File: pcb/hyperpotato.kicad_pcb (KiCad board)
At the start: 2 copper layers, 117 x 88.3 mm, 46 parts, among them J1 Conn_01x02_Socket, J2 Conn_01x03_Pin, Q1 AO3401A, SW1 SW_Push_45deg, SW10 SW_Push_45deg, SW11 SW_Push_45deg, SW12 SW_Push_45deg, SW13 SW_Push_45deg, SW14 SW_SPDT, SW15 SW_Push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

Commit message: Route haptic driver
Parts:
- U1: footprint ssbb_parts:Xiao_nRF52840_AC_Reflow_reversible -> hyperpotato:Xiao_nRF52840_AC_Reflow_reversible
- moved U4 61.0 mm to (140.2, 87.3), turned to 180 degrees
- moved U1 16.7 mm to (145.1, 61.4), turned to 0 degrees
- moved SW14 16.5 mm to (165.5, 54.3), turned to 180 degrees
- moved SW1 15.5 mm to (165.5, 67.0), turned to 0 degrees
- moved SW2 15.3 mm to (187.2, 61.0), turned to -5 degrees
- moved SW15 15.3 mm to (205.6, 56.8), turned to 175 degrees
- moved U5 15.2 mm to (145.1, 79.4), turned to -90 degrees
- moved D14 15.1 mm to (220.3, 57.2), turned to -140 degrees
- moved R6 14.8 mm to (216.0, 60.7), turned to -50 degrees
- moved D15 14.7 mm to (223.8, 61.4), turned to -140 degrees
- moved R7 14.4 mm to (219.6, 65.0), turned to -50 degrees
- moved D16 14.3 mm to (227.4, 65.7), turned to -140 degrees
- moved SW3 14.3 mm to (204.5, 69.4), turned to 175 degrees
- moved SW6 14.2 mm to (165.5, 84.0), turned to 0 degrees
- moved R8 14.0 mm to (223.1, 69.3), turned to -50 degrees
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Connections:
- U5 pad 1: COL0 -> COL3
- U5 pad 15: LED1 -> COL0
- U5 pad 3: COL3 -> LED3
- U5 pad 4: COL2 -> LED2
- U5 pad 5: COL1 -> LED1
- U5 pad 6: LED2 -> COL2
- U5 pad 7: LED3 -> COL1
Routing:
- net +3.3V: track 11.1 -> 98.7 mm, vias 0 -> 8
- net ROW0: track 111.7 -> 164.3 mm, vias 5 -> 7
- net ROW2: track 112.8 -> 163.7 mm, vias 5 -> 7
- net ROW1: track 117.7 -> 168.2 mm, vias 7 -> 9
- net IO_CS: track 0.00 -> 43.0 mm, vias 0 -> 2
- net LED1: track 47.1 -> 90.0 mm, vias 1 -> 2
- net LED2: track 51.2 -> 91.8 mm, vias 1 -> 2
- net SCK: track 0.00 -> 40.6 mm, vias 0 -> 2
- net LED3: track 55.6 -> 96.1 mm, vias 1 -> 2
- net MOSI: track 0.00 -> 39.6 mm, vias 0 -> 2
- net COL0: track 2.27 -> 39.7 mm, vias 0 -> 1
- net TP_DATA: track 0.00 -> 37.0 mm, vias 0 -> 2
- net RESET: track 43.2 -> 79.0 mm, vias 1 -> 3
- net TP_CLK: track 0.00 -> 32.7 mm, vias 0 -> 2
- net TP_RST: track 0.00 -> 28.6 mm, vias 0 -> 2
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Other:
- board size 117 x 88.3 mm -> 115 x 90.8 mm

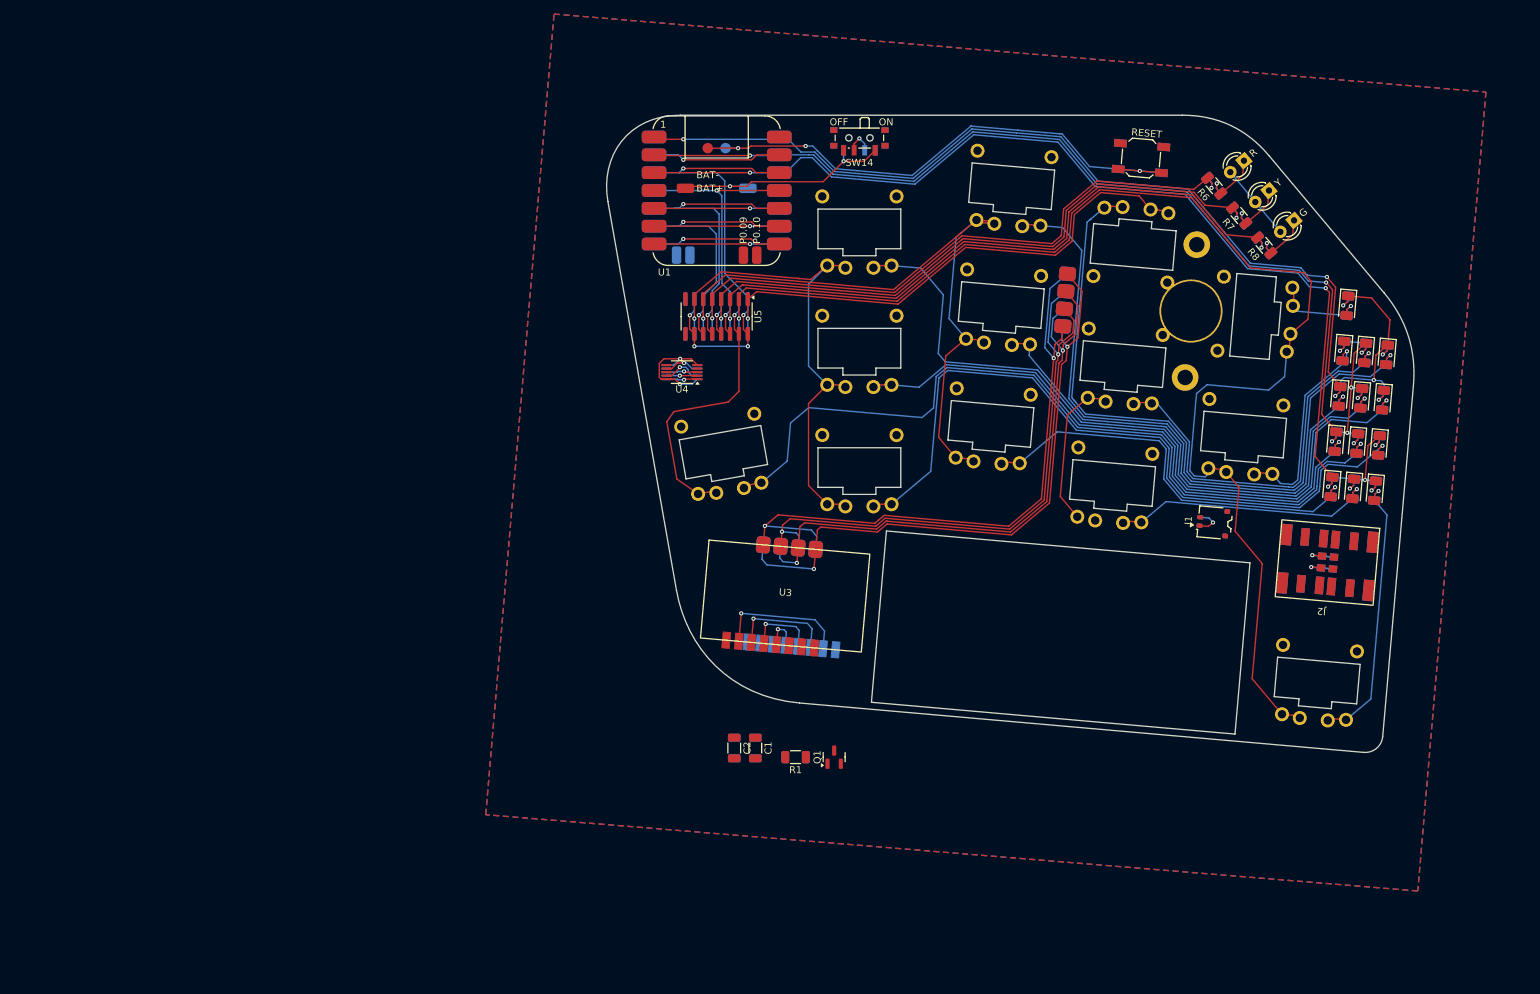
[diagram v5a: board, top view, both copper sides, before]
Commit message: Almost routed, changing 595 package
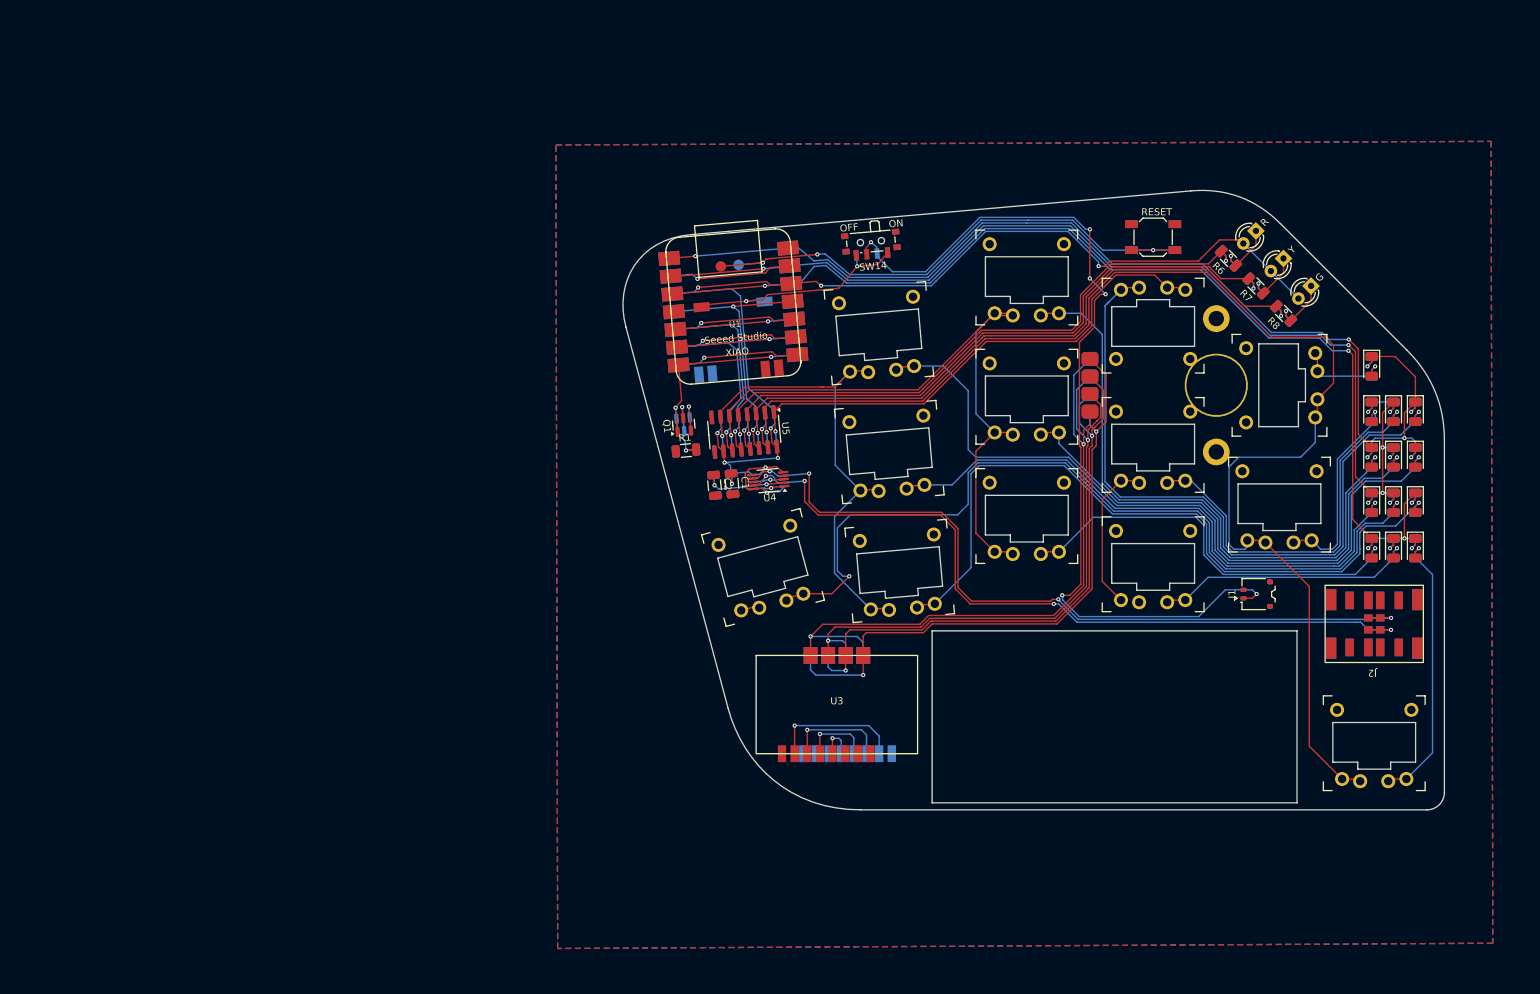
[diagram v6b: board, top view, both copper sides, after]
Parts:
- Q1: footprint Package_TO_SOT_SMD:SOT-23 -> hyperpotato:SOT-23_reversible
- SW1, SW10, SW11, SW12, SW13, SW2, SW3, SW4, SW5, SW6, SW7, SW8, SW9: footprint ssbb_parts:SW_Choc_Mini_reversible_1u -> hyperpotato:SW_Choc_Mini_reversible_1u
- U1: footprint hyperpotato:Xiao_nRF52840_AC_Reflow_reversible -> hyperpotato:XIAO-nRF52840-Sense-14P-2.54-21X17.8MM_1
- moved Q1 52.0 mm to (140.4, 94.8), turned to 95 degrees
- moved R1 46.4 mm to (140.8, 98.5), turned to 5 degrees
- moved C2 37.9 mm to (144.8, 103.4), turned to -85 degrees
- moved C1 37.6 mm to (147.3, 103.2), turned to -85 degrees
- moved U4 19.8 mm to (152.5, 102.8), turned to -175 degrees
- moved SW5 17.2 mm to (151.7, 115.1), turned to 15 degrees
- moved U3 17.1 mm to (162.3, 134.7), turned to 0 degrees
- moved U5 16.9 mm to (149.1, 95.8), turned to -85 degrees
- moved U1 16.7 mm to (147.5, 78.0), turned to 5 degrees
- moved SW10 15.7 mm to (171.2, 115.6), turned to 5 degrees
- moved SW6 15.3 mm to (169.7, 98.7), turned to 5 degrees
- moved SW1 15.0 mm to (168.2, 81.8), turned to 5 degrees
- moved SW14 14.9 mm to (167.1, 69.1), turned to -175 degrees
- moved SW11 14.0 mm to (189.3, 107.8), turned to 0 degrees
- moved SW7 13.4 mm to (189.3, 90.8), turned to 0 degrees
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- renumbered C2 to C1, C1 to C2
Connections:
- C1 pad 1: Net-(U4-REG) -> +3.3V
- C2 pad 1: +3.3V -> Net-(U4-REG)
- U3 pad 5: +3.3V -> +3.3V_OPTIONAL
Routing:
- net VBAT: track 8.23 -> 129.2 mm, vias 2 -> 6
- net Net-(J2-Pin_2): track 11.3 -> 111.1 mm, vias 2 -> 4
- net Net-(J2-Pin_1): track 12.0 -> 111.1 mm, vias 2 -> 4
- net +3.3V: track 98.7 -> 177.2 mm, vias 8 -> 11
- net COL0: track 39.7 -> 7.75 mm
- net POWER_CUTOFF: track 17.8 -> 37.2 mm, vias 1 -> 3
- net +3.3V_OPTIONAL: track 0.00 -> 10.5 mm, vias 0 -> 2
- net Net-(U4-REG): track 4.48 -> 13.3 mm, vias 1 -> 2
- net Net-(D5-A): track 117.0 -> 120.7 mm, vias 1 -> 2
- net ROW0: track 164.3 -> 162.3 mm
- net RESET: track 79.0 -> 80.7 mm
- net COL4: track 188.0 -> 186.4 mm
- net LED1: track 90.0 -> 88.7 mm
- net +BATT: track 33.5 -> 32.3 mm
- net LED3: track 96.1 -> 95.1 mm
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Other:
- board size 115 x 90.8 mm -> 117 x 88.3 mm

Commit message: Good progress on routing
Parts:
- U5: footprint ssbb_parts_reversible:SOIC-16_3.9x9.9mm_P1.27mm_reversible -> ssbb_parts_reversible:TSSOP-16_4.4x5mm_P0.65mm_reversible
- moved R1 13.5 mm to (151.7, 106.3), turned to 0 degrees
- moved Q1 13.5 mm to (151.7, 102.1), turned to 90 degrees
- moved U5 9.86 mm to (158.2, 99.5), turned to -90 degrees
- moved U4 6.71 mm to (148.5, 97.4), turned to 0 degrees
- moved C1 3.81 mm to (148.4, 102.1), turned to -90 degrees
- moved D2 3.51 mm to (241.4, 101.3)
- moved J1 3.51 mm to (225.0, 120.8)
- moved SW8 3.51 mm to (210.3, 99.6)
- moved D13 3.51 mm to (247.6, 114.3)
- moved SW14 3.51 mm to (170.1, 71.0)
- moved SW5 3.51 mm to (154.7, 117.0)
- moved R8 3.51 mm to (228.8, 80.9)
- moved SW6 3.51 mm to (172.7, 100.6)
- moved SW15 3.51 mm to (210.3, 70.0)
- moved D15 3.51 mm to (228.8, 73.0)
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- renumbered C2 to C1, C1 to C2
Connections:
- C1 pad 1: Net-(U4-REG) -> +3.3V
- C2 pad 1: +3.3V -> Net-(U4-REG)
- U1 pad 11: MOSI -> SCK
- U1 pad 13: SCK -> MOSI
- U1 pad 14: TP_RST -> POWER_CUTOFF
- U1 pad 7: POWER_CUTOFF -> TP_RST
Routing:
- net TP_DATA: track 37.0 -> 100.9 mm
- net TP_CLK: track 32.7 -> 93.0 mm
- net TP_RST: track 28.6 -> 87.3 mm
- net +3.3V_OPTIONAL: track 10.5 -> 61.5 mm
- net +3.3V: track 177.2 -> 198.6 mm, vias 11 -> 12
- net COL1: track 72.8 -> 90.3 mm
- net MOSI: track 39.6 -> 55.1 mm, vias 2 -> 3
- net Net-(J2-Pin_1): track 111.1 -> 126.3 mm
- net SCK: track 40.1 -> 55.2 mm, vias 2 -> 3
- net Net-(J2-Pin_2): track 111.1 -> 124.6 mm
- net COL2: track 96.1 -> 108.9 mm
- net LED1: track 88.7 -> 101.4 mm
- net IO_CS: track 43.0 -> 55.4 mm, vias 2 -> 3
- net SDA: track 4.48 -> 16.3 mm, vias 1 -> 2
- net LED2: track 91.1 -> 101.1 mm
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
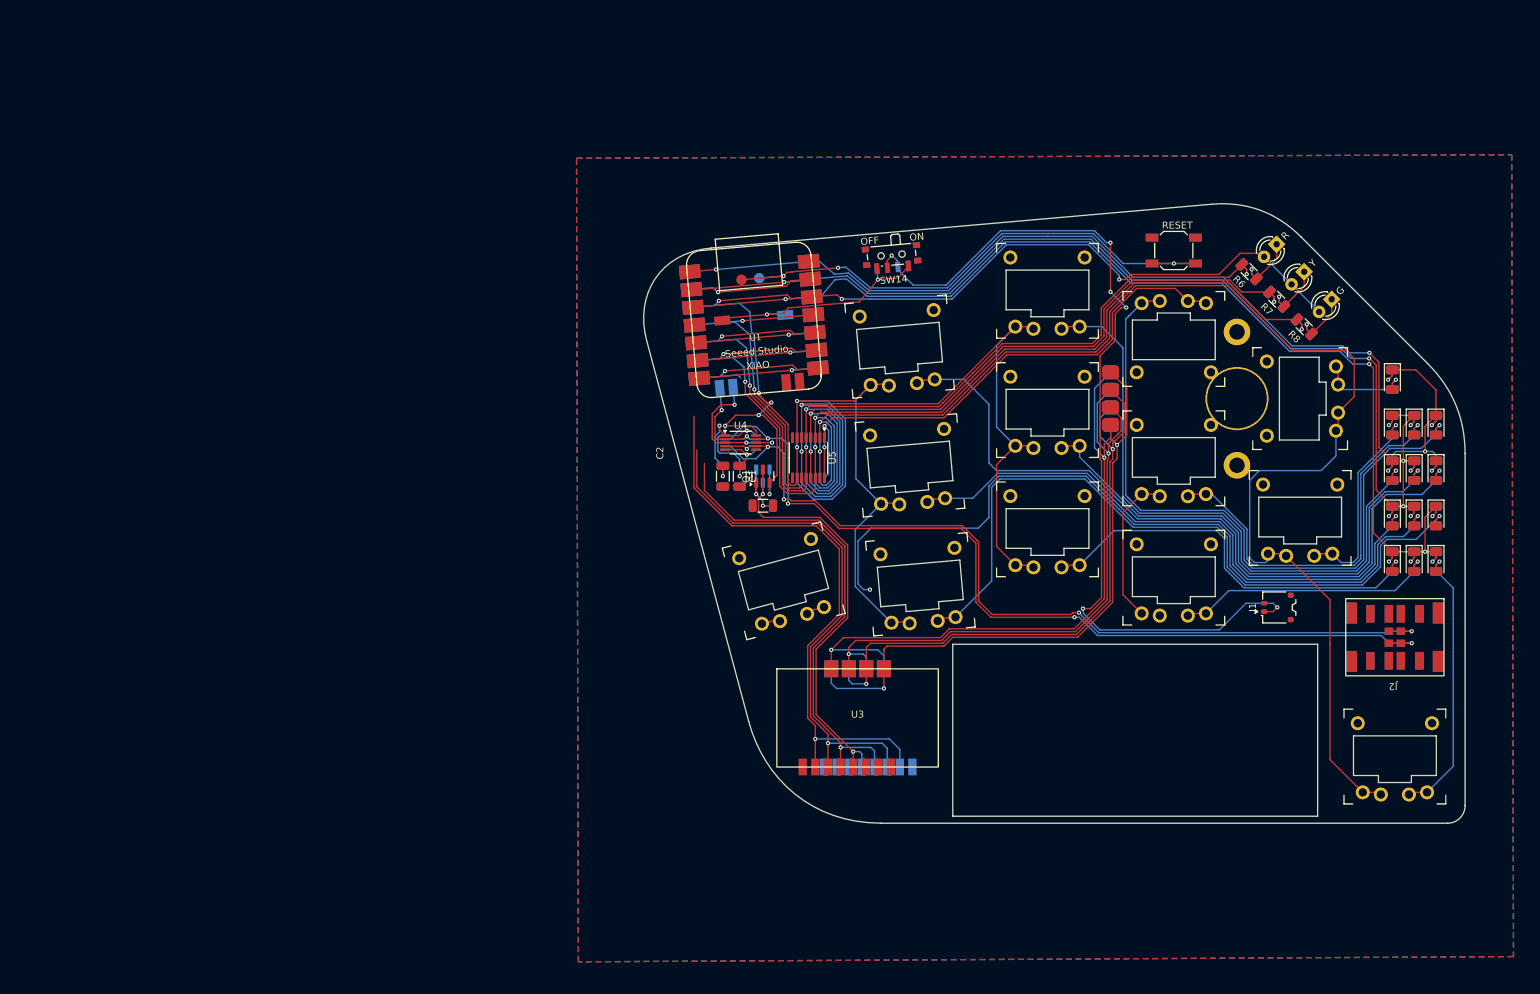
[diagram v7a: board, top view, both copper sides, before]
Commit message: Use in-house footprints,
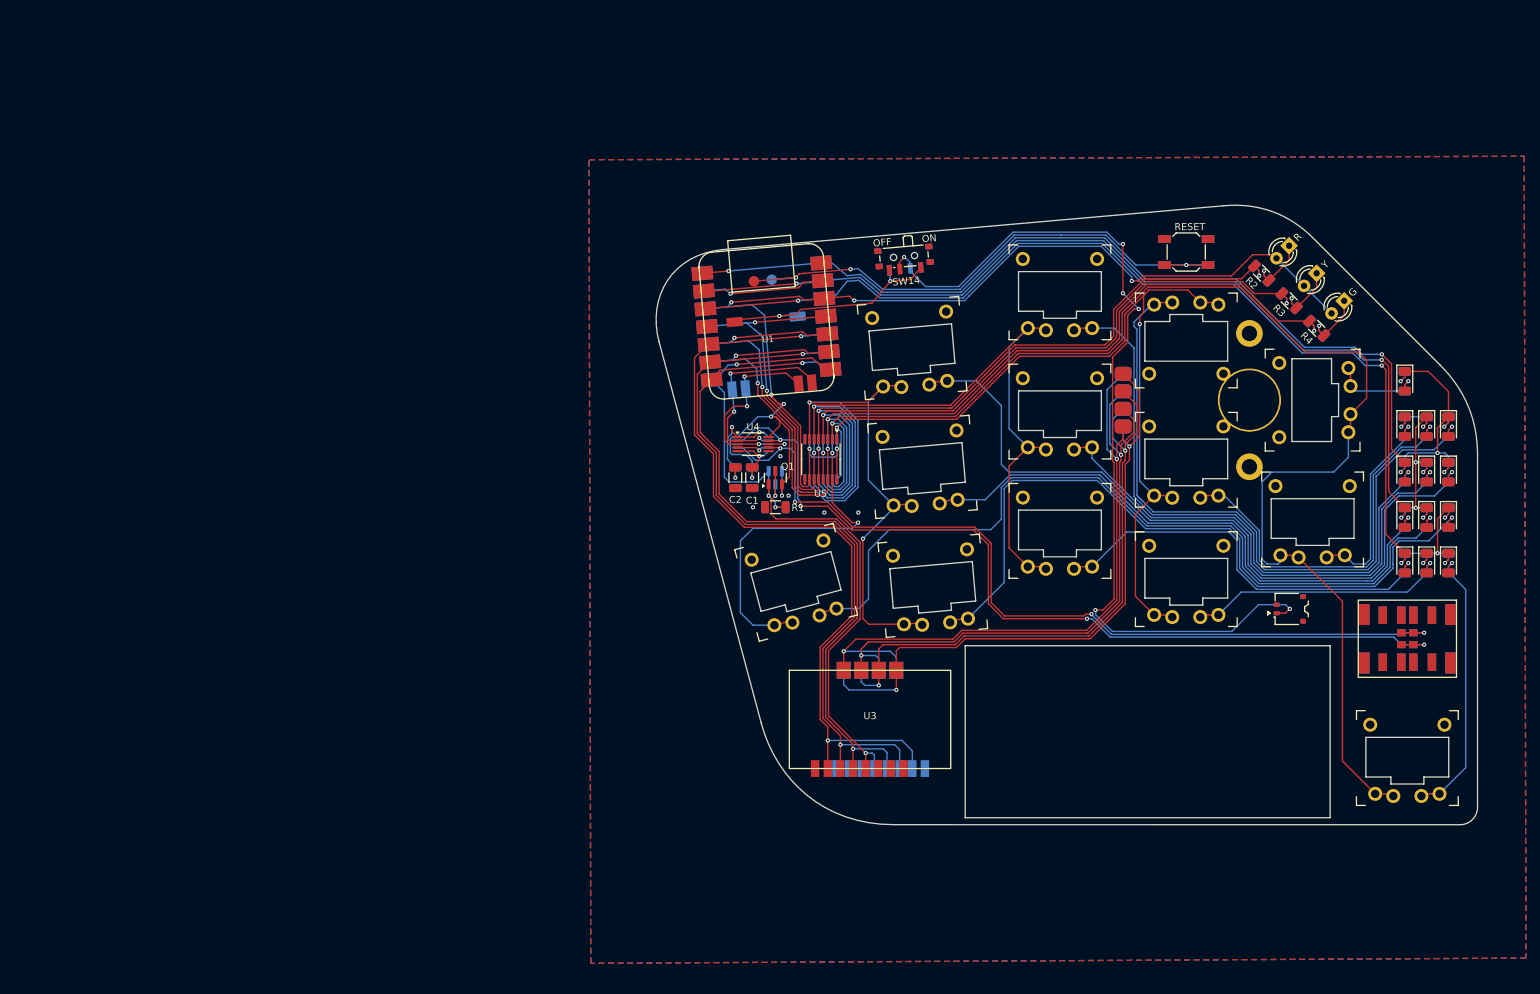
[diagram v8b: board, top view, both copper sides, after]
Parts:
- D9: moved to F.Cu
- H1: value MountingHole -> T460S
- U1: footprint hyperpotato:XIAO-nRF52840-Sense-14P-2.54-21X17.8MM_1 -> hyperpotato:XIAO-nRF52840-Sense-14P-2.54-21X17.8MM_reversible
- moved D2 1.79 mm to (243.2, 101.6)
- moved SW15 1.79 mm to (212.0, 70.2)
- moved D4 1.79 mm to (243.2, 88.6)
- moved R2 1.79 mm to (222.8, 73.2)
- moved SW5 1.79 mm to (156.5, 117.3)
- moved R1 1.79 mm to (153.5, 106.6)
- moved J1 1.79 mm to (226.8, 121.1)
- moved SW2 1.79 mm to (194.0, 75.9)
- moved Q1 1.79 mm to (153.5, 102.4)
- moved U1 1.79 mm to (152.2, 80.1)
- moved SW10 1.79 mm to (175.9, 117.8)
- moved SW1 1.79 mm to (173.0, 83.9)
- moved D11 1.79 mm to (243.2, 114.5)
- moved D16 1.79 mm to (234.5, 77.1)
- moved D8 1.79 mm to (246.3, 95.1)
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- renumbered R6 to R2, R7 to R3, R8 to R4
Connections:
- U1 pad 17: SCL -> SDA
- U1 pad 18: SDA -> SCL
- U1 pad 5: TP_CLK -> TP_DATA
- U1 pad 6: TP_DATA -> TP_CLK
- U3 pad 10: TP_S2 -> TP_GND
- U3 pad 11: TP_S3 -> TP_Y
- U3 pad 12: TP_S4 -> TP_X
- U3 pad 9: TP_S1 -> TP_VCC
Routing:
- net COL0: track 7.99 -> 49.8 mm, vias 1 -> 2
- net COL3: track 96.1 -> 128.2 mm, vias 1 -> 2
- net POWER_CUTOFF: track 31.6 -> 49.2 mm
- net SCL: track 13.7 -> 28.2 mm, vias 2 -> 3
- net TP_CLK: track 93.0 -> 107.5 mm
- net TP_RST: track 87.3 -> 101.0 mm
- net TP_DATA: track 100.9 -> 113.2 mm
- net SDA: track 16.3 -> 26.3 mm, vias 2 -> 3
- net Net-(D5-A): track 113.2 -> 117.8 mm, vias 2 -> 1
- net COL1: track 90.3 -> 93.4 mm, vias 1 -> 2
- net +3.3V: track 198.6 -> 201.1 mm, vias 12 -> 11
- net MOSI: track 55.1 -> 54.5 mm
- net GND: vias 4 -> 9
